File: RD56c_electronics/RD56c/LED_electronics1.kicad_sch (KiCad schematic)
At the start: 12 parts, among them IC1 STP24DP05BTR, IC2 STP24DP05BTR

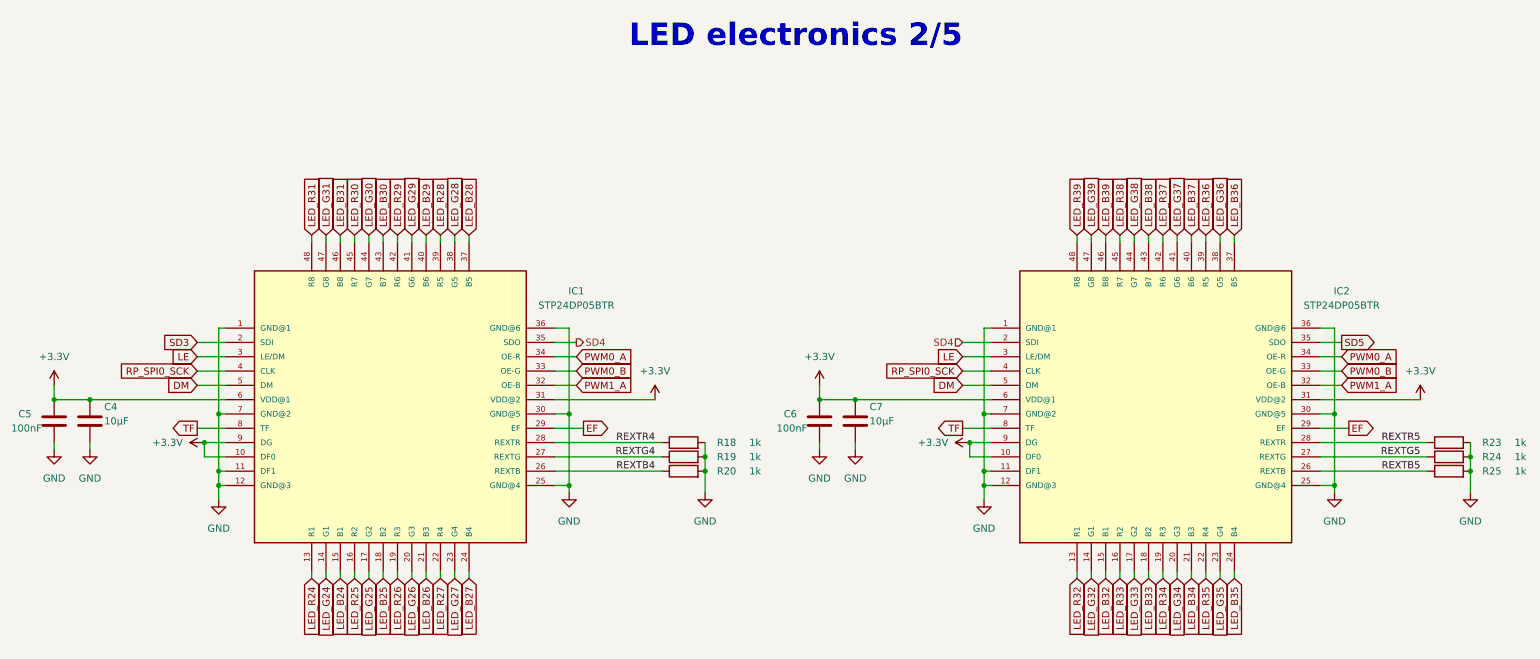
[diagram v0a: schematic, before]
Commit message: added empty_sheet.kicad_wks to KiCAD folders
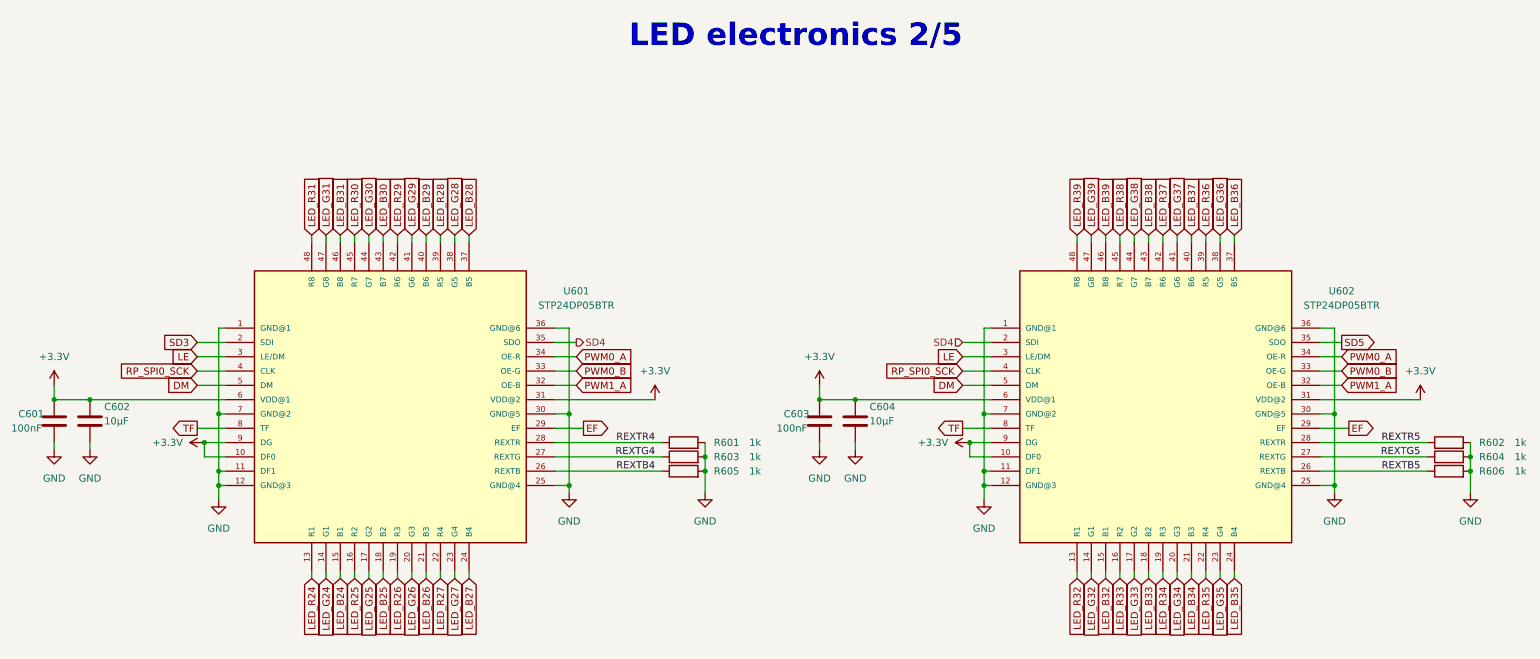
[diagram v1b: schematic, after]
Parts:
- renumbered C5 to C601, C4 to C602, C6 to C603, C7 to C604, R18 to R601, R23 to R602, R19 to R603, R24 to R604, R20 to R605, R25 to R606, IC1 to U601, IC2 to U602
